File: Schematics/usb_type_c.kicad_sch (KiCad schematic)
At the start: 4 parts, among them J2 USB_C_Receptacle

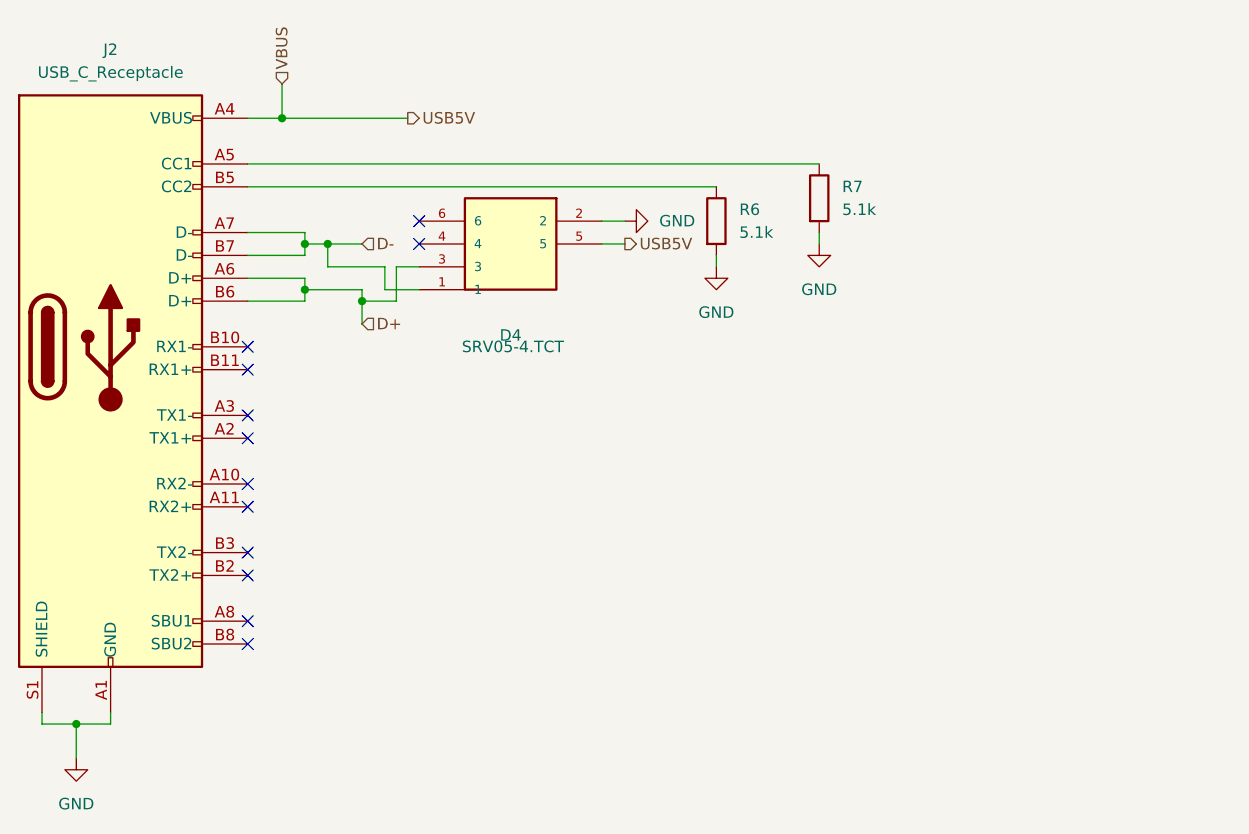
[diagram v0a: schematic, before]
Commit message: added esp32 for uart to tune control systems from a web browser app
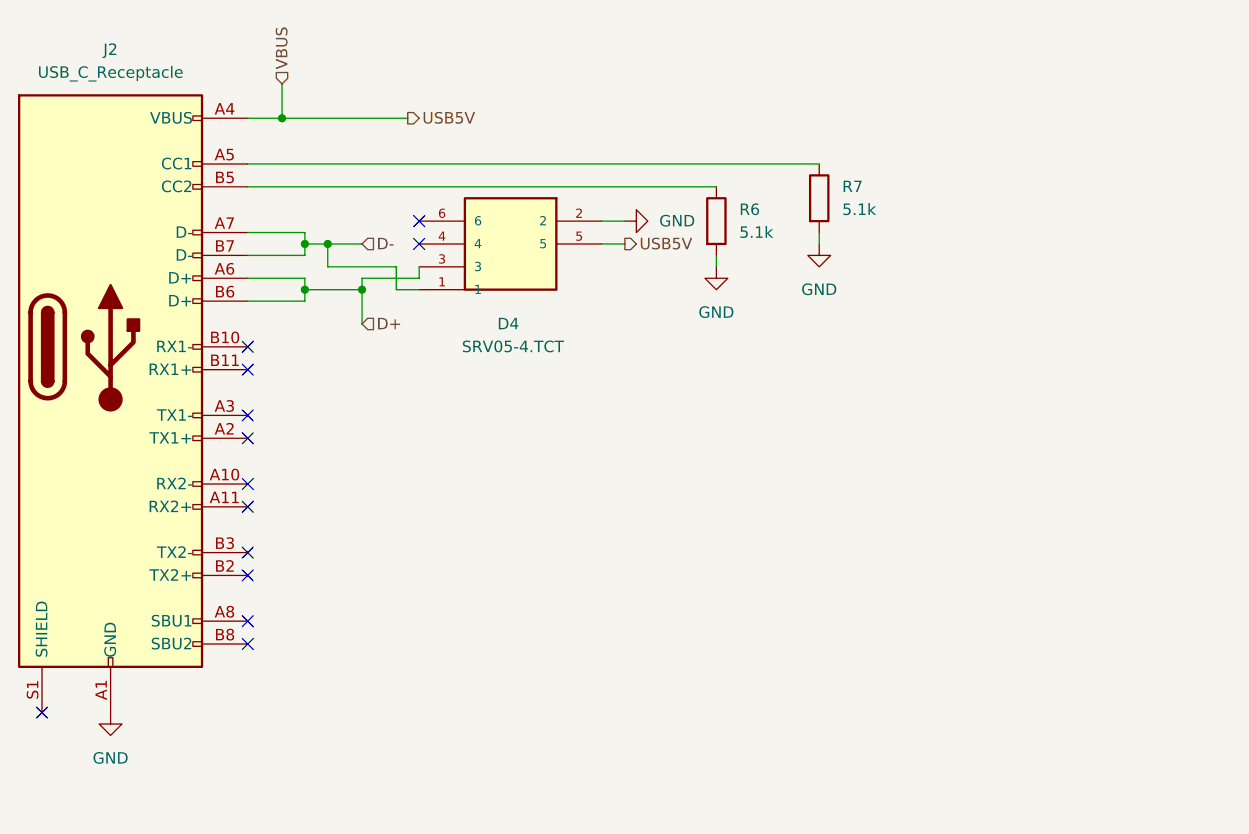
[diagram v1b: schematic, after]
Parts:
- D4: footprint custom footprints:SOT-23-6_L2.9-W1.6-P0.95-LS2.8-BR -> Package_TO_SOT_SMD:SOT-23-6
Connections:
- net GND: no longer J2.S1 (SHIELD)
- no-connect marks 12 -> 13
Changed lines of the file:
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@@
-	)
-	(junction
-		(at 110.49 91.44)
-		(diameter 0)
-		(color 0 0 0 0)
-	)
-	(junction
-		(at 78.74 138.43)
-		(diameter 0)
-		(color 0 0 0 0)
 	)
 	(junction
@@
 	)
 	(junction
+		(at 110.49 90.17)
+		(diameter 0)
+		(color 0 0 0 0)
+	)
+	(junction
 		(at 104.14 90.17)
 		(diameter 0)
@@
 	)
 	(no_connect
+		(at 74.93 137.16)
+	)
+	(no_connect
 		(at 97.79 106.68)
 	)
@@
 	(wire
 		(pts
-			(xy 113.03 90.17) (xy 113.03 87.63)
-		)
-		(stroke
-			(width 0)
-			(type default)
-		)
-	)
-	(wire
-		(pts
-			(xy 78.74 138.43) (xy 82.55 138.43)
-		)
-		(stroke
-			(width 0)
-			(type default)
-		)
-	)
-	(wire
-		(pts
 			(xy 104.14 91.44) (xy 97.79 91.44)
 		)
@@
 	(wire
 		(pts
-			(xy 116.84 90.17) (xy 113.03 90.17)
-		)
-		(stroke
-			(width 0)
-			(type default)
-		)
-	)
-	(wire
-		(pts
 			(xy 104.14 85.09) (xy 106.68 85.09)
 		)
@@
 	(wire
 		(pts
-			(xy 114.3 91.44) (xy 110.49 91.44)
-		)
-		(stroke
-			(width 0)
-			(type default)
-		)
-	)
-	(wire
-		(pts
 			(xy 149.86 86.36) (xy 149.86 87.63)
 		)
@@
 	(wire
 		(pts
+			(xy 114.3 87.63) (xy 114.3 90.17)
+		)
+		(stroke
+			(width 0)
+			(type default)
+		)
+	)
+	(wire
+		(pts
 			(xy 104.14 83.82) (xy 104.14 85.09)
 		)
@@
 	(wire
 		(pts
-			(xy 78.74 138.43) (xy 78.74 142.24)
-		)
-		(stroke
-			(width 0)
-			(type default)
-		)
-	)
-	(wire
-		(pts
-			(xy 114.3 87.63) (xy 114.3 91.44)
-		)
-		(stroke
-			(width 0)
-			(type default)
-		)
-	)
-	(wire
-		(pts
 			(xy 106.68 85.09) (xy 110.49 85.09)
 		)
@@
 	(wire
 		(pts
-			(xy 110.49 91.44) (xy 110.49 90.17)
+			(xy 106.68 87.63) (xy 114.3 87.63)
 		)
 		(stroke
@@
 	(wire
 		(pts
+			(xy 110.49 88.9) (xy 116.84 88.9)
+		)
+		(stroke
+			(width 0)
+			(type default)
+		)
+	)
+	(wire
+		(pts
 			(xy 101.6 71.12) (xy 115.57 71.12)
 		)
@@
 	(wire
 		(pts
+			(xy 110.49 90.17) (xy 110.49 88.9)
+		)
+		(stroke
+			(width 0)
+			(type default)
+		)
+	)
+	(wire
+		(pts
 			(xy 97.79 76.2) (xy 161.29 76.2)
 		)
@@
 	(wire
 		(pts
-			(xy 110.49 93.98) (xy 110.49 91.44)
-		)
-		(stroke
-			(width 0)
-			(type default)
-		)
-	)
-	(wire
-		(pts
-			(xy 113.03 87.63) (xy 106.68 87.63)
-		)
-		(stroke
-			(width 0)
-			(type default)
-		)
-	)
-	(wire
-		(pts
-			(xy 74.93 138.43) (xy 78.74 138.43)
+			(xy 110.49 90.17) (xy 110.49 93.98)
 		)
 		(stroke
@@
 	(wire
 		(pts
-			(xy 116.84 87.63) (xy 114.3 87.63)
-		)
-		(stroke
-			(width 0)
-			(type default)
-		)
-	)
-	(wire
-		(pts
 			(xy 139.7 82.55) (xy 137.16 82.55)
 		)
@@
 	(wire
 		(pts
-			(xy 74.93 138.43) (xy 74.93 137.16)
-		)
-		(stroke
-			(width 0)
-			(type default)
-		)
-	)
-	(wire
-		(pts
 			(xy 104.14 86.36) (xy 97.79 86.36)
 		)
@@
 	(wire
 		(pts
-			(xy 82.55 138.43) (xy 82.55 137.16)
+			(xy 116.84 88.9) (xy 116.84 87.63)
+		)
+		(stroke
+			(width 0)
+			(type default)
+		)
+	)
+	(wire
+		(pts
+			(xy 114.3 90.17) (xy 116.84 90.17)
 		)
 		(stroke
@@
 	)
 	(symbol
+		(lib_id "power:GND")
+		(at 82.55 137.16 0)
+		(unit 1)
+		(exclude_from_sim no)
+		(in_bom yes)
+		(on_board yes)
+		(dnp no)
+		(fields_autoplaced yes)
+		(property "Reference" "#PWR04"
+			(at 82.55 143.51 0)
+			(effects
+				(font
+					(size 1.27 1.27)
+				)
+				(hide yes)
+			)
+		)
+		(property "Value" "GND"
+			(at 82.55 142.24 0)
+			(effects
+				(font
+					(size 1.27 1.27)
+				)
+			)
+		)
+		(property "Footprint" ""
+			(at 82.55 137.16 0)
+			(effects
+				(font
+					(size 1.27 1.27)
+				)
+				(hide yes)
+			)
+		)
+		(property "Datasheet" ""
+			(at 82.55 137.16 0)
+			(effects
+				(font
+					(size 1.27 1.27)
+				)
+				(hide yes)
+			)
+		)
+		(property "Description" "Power symbol creates a global label with name \"GND\" , ground"
+			(at 82.55 137.16 0)
+			(effects
+				(font
+					(size 1.27 1.27)
+				)
+				(hide yes)
+			)
+		)
+		(pin "1"
+		)
+		(instances
+			(project ""
+				(path "/8a3e7f99-4046-40e8-bd7c-d9d1c8c7162e/f33094e5-7720-4bb5-9ddf-b2cfd7a85122"
+					(reference "#PWR04")
+					(unit 1)
+				)
+			)
+		)
+	)
+	(symbol
 		(lib_id "SRV05-4.TCT:SRV05-4.TCT")
 		(at 137.16 87.63 180)
@@
 		(dnp no)
 		(property "Reference" "D4"
-			(at 127 95.25 0)
+			(at 126.746 93.98 0)
 			(effects
 				(font
@@
 			)
 		)
-		(property "Footprint" "custom footprints:SOT-23-6_L2.9-W1.6-P0.95-LS2.8-BR"
+		(property "Footprint" "Package_TO_SOT_SMD:SOT-23-6"
 			(at 137.16 87.63 0)
 			(effects
@@
 					(unit 1)
 				)
-			)
-		)
-	)
-	(symbol
-		(lib_id "power:GND")
-		(at 78.74 142.24 0)
-		(unit 1)
-		(exclude_from_sim no)
-		(in_bom yes)
-		(on_board yes)
-		(dnp no)
-		(fields_autoplaced yes)
-		(property "Reference" "#PWR058"
-			(at 78.74 148.59 0)
-			(effects
-				(font
-					(size 1.27 1.27)
-				)
-				(hide yes)
-			)
-		)
-		(property "Value" "GND"
-			(at 78.74 147.32 0)
-			(effects
-				(font
-					(size 1.27 1.27)
-				)
-			)
-		)
-		(property "Footprint" ""
-			(at 78.74 142.24 0)
-			(effects
-				(font
-					(size 1.27 1.27)
-				)
-				(hide yes)
-			)
-		)
-		(property "Datasheet" ""
-			(at 78.74 142.24 0)
-			(effects
-				(font
-					(size 1.27 1.27)
-				)
-				(hide yes)
-			)
-		)
-		(property "Description" "Power symbol creates a global label with name \"GND\" , ground"
-			(at 78.74 142.24 0)
-			(effects
-				(font
-					(size 1.27 1.27)
-				)
-				(hide yes)
-			)
-		)
-		(pin "1"
-		)
-		(instances
-			(project ""
-				(path "/65068a32-f105-4204-b50e-234054c5a6d0/880da092-1c6b-4dcf-a509-490b22fc0ebc"
-					(reference "#PWR047")
-					(unit 1)
-				)
-			)
-			(project "CAN-Interface-Board"
-				(path "/8a3e7f99-4046-40e8-bd7c-d9d1c8c7162e/f33094e5-7720-4bb5-9ddf-b2cfd7a85122"
-					(reference "#PWR058")
-					(unit 1)
-				)

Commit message: updated board waiting on review
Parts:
- D4: DESCRIPTION Semtech SRV05-4.TCT, Uni-Directional TVS Diode Array, 300W,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 -> (none)

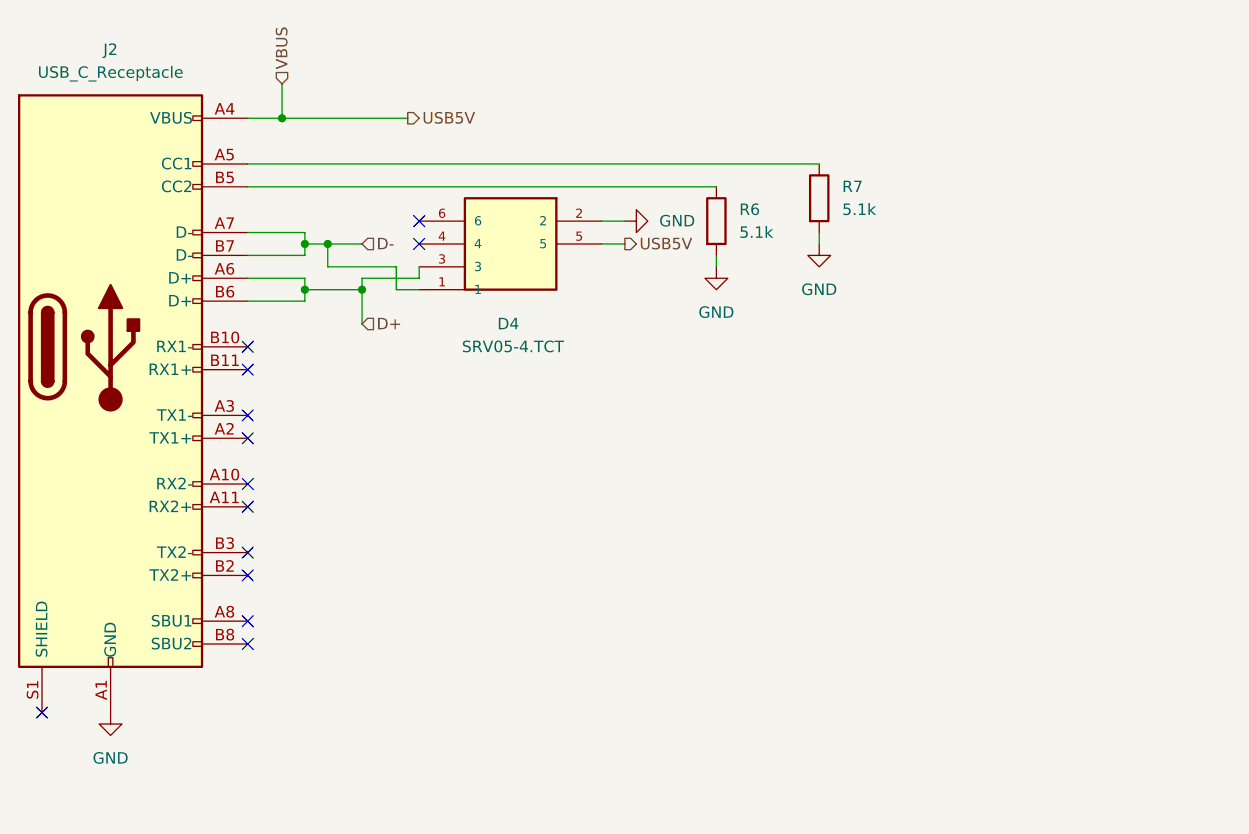
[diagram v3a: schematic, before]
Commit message: Added encoder connection for parafoil motor position information, in buy order ready for purchase
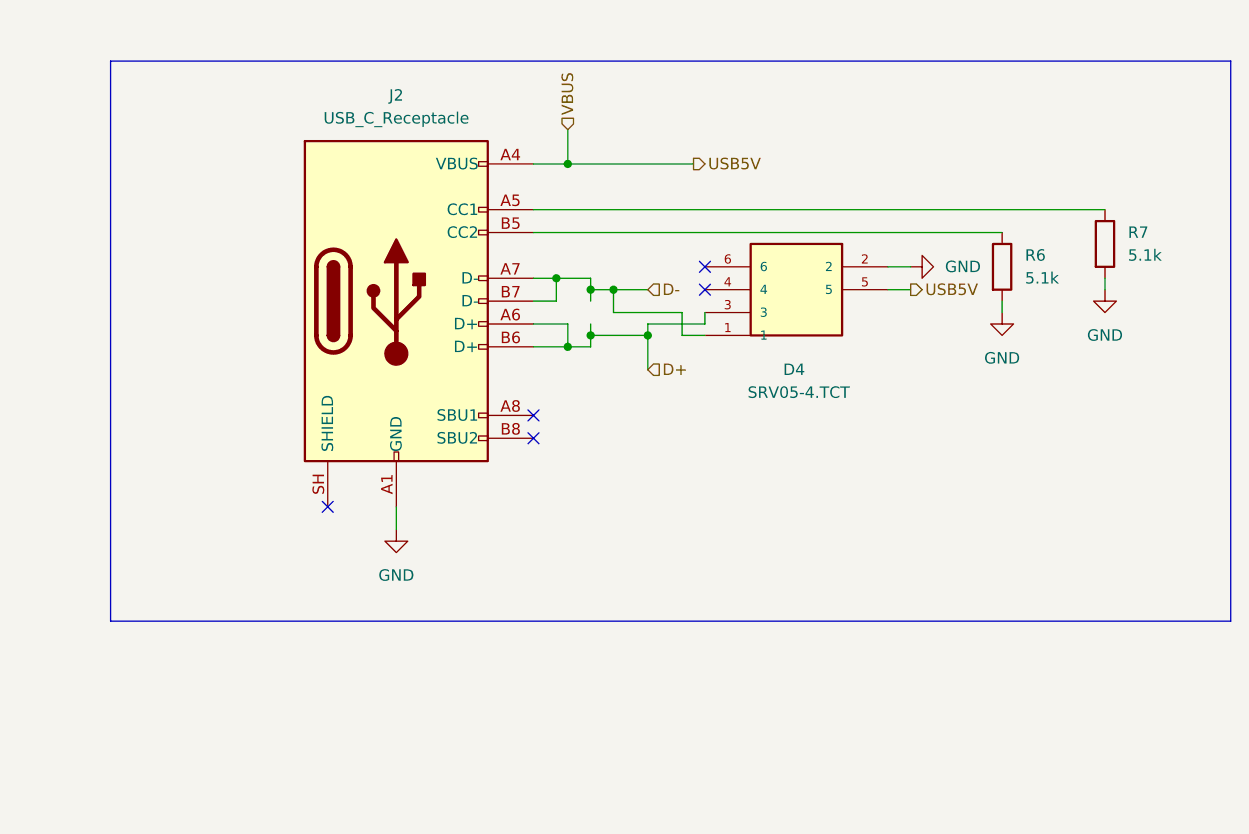
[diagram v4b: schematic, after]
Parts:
- J2: symbol Connector:USB_C_Receptacle -> Connector:USB_C_Receptacle_USB2.0_16P; LCSC C49566391 -> C165948
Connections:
- no-connect marks 13 -> 5
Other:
- moved on the sheet: D4, R6, R7
